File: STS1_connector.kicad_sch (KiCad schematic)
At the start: 2 parts

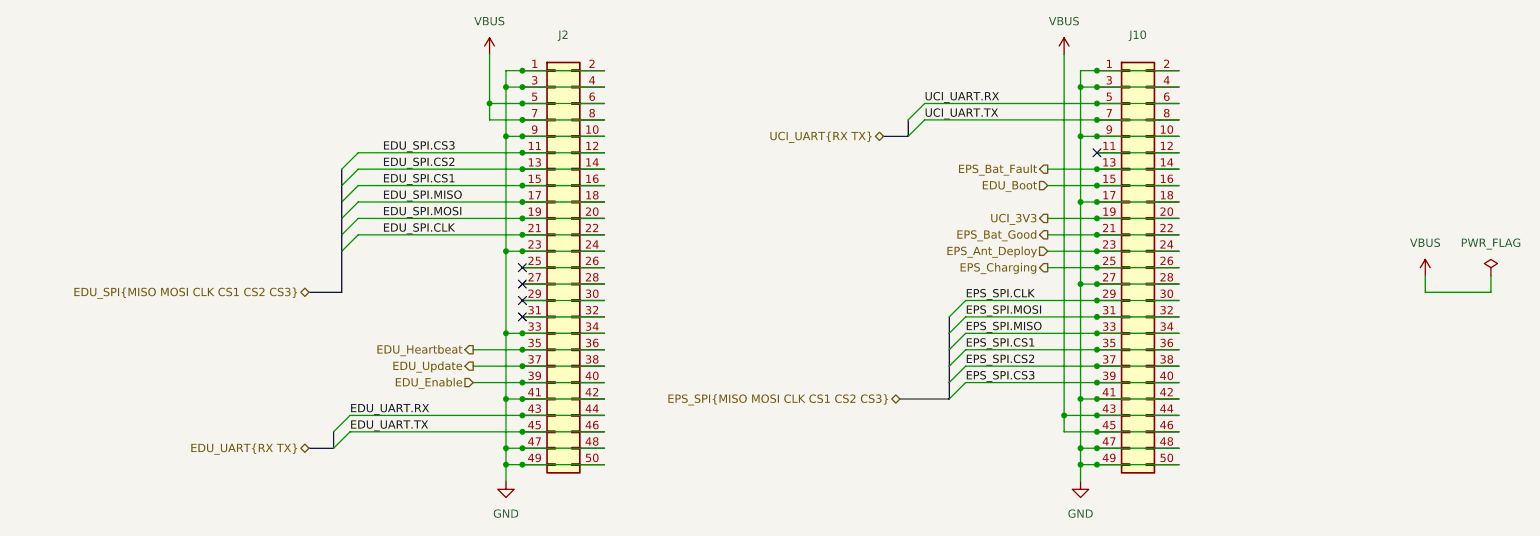
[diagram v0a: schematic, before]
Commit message: Reorganize and clean-up the components around the STM. Pinout changes: 1) Flash_CS moved from PB9 to PA4 2) Dosi_En added on PB10 3) EDU_Boot_Pin added on PB2 4) WDT_Clear moved from PA9 to PB9
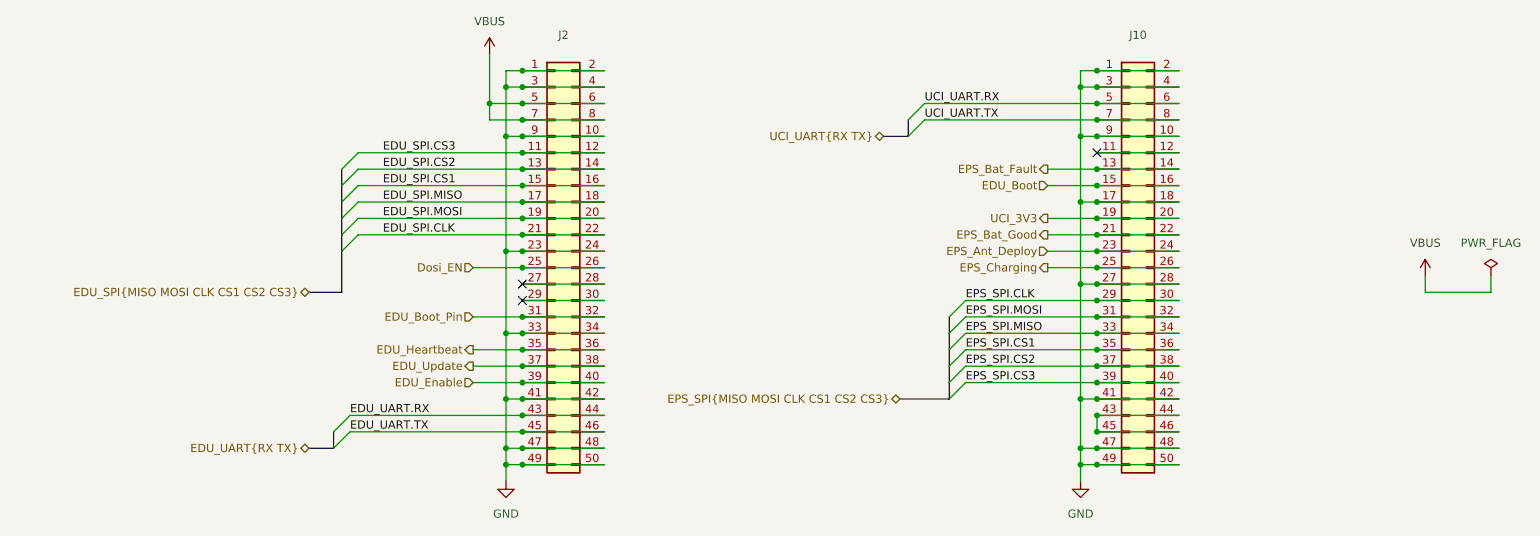
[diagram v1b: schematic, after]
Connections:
- net VBUS: no longer J10.43 (Pin_43), J10.44 (Pin_44), J10.45 (Pin_45), J10.46 (Pin_46)
- net Dosi_EN: now reaches J2.25 (Pin_25), J2.26 (Pin_26)
- net EDU_Boot_Pin: now reaches J2.31 (Pin_31), J2.32 (Pin_32)
- new net: J10.43 (Pin_43), J10.44 (Pin_44), J10.45 (Pin_45), J10.46 (Pin_46)
- no-connect marks 5 -> 3

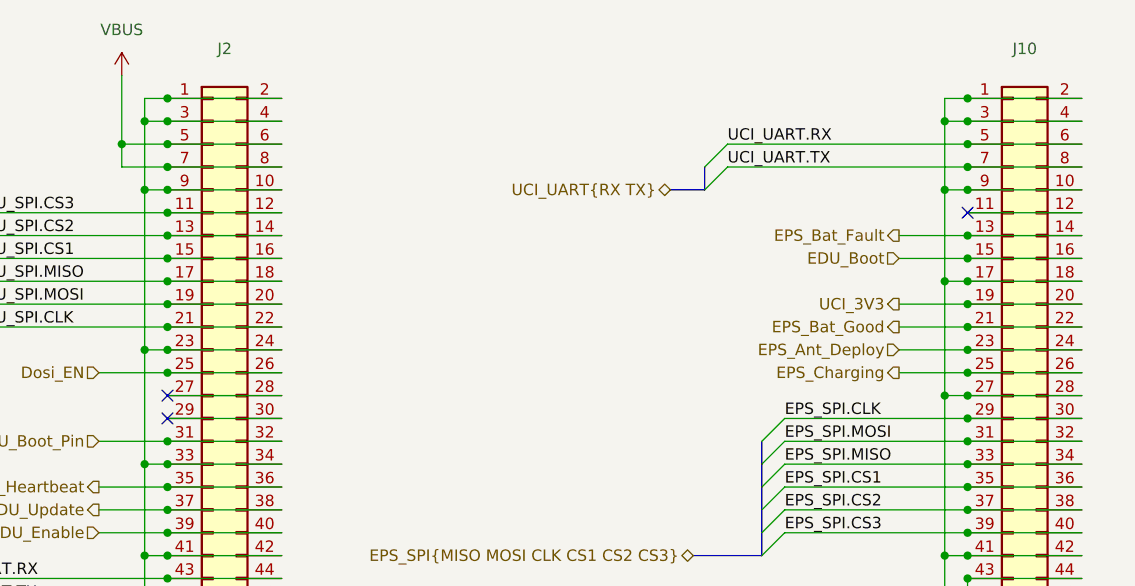
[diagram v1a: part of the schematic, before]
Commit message: Add latchup protection circuits
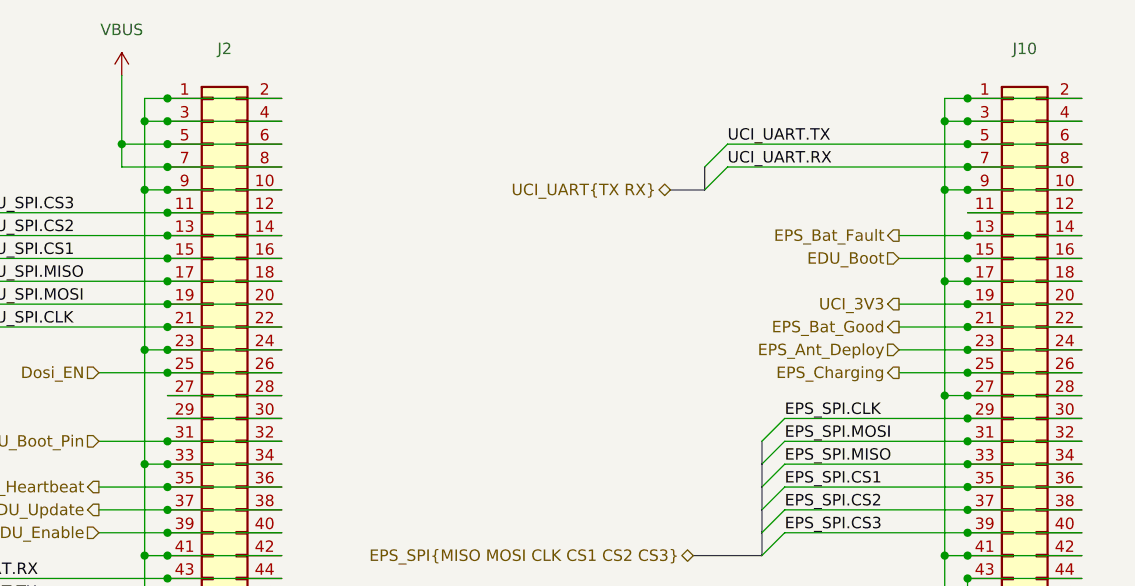
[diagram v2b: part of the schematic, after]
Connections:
- net UCI_UART.RX: now also J10.7 (Pin_7), J10.8 (Pin_8); no longer J10.5 (Pin_5), J10.6 (Pin_6)
- net UCI_UART.TX: now also J10.5 (Pin_5), J10.6 (Pin_6); no longer J10.7 (Pin_7), J10.8 (Pin_8)
- no-connect marks 3 -> 0
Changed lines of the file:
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@@
   (junction (at 173.99 96.52) (diameter 0) (color 0 0 0 0)
   )
-  (no_connect (at 85.09 81.28))
-  (no_connect (at 85.09 78.74))
-  (no_connect (at 173.99 58.42))
   (bus_entry (at 151.13 93.98) (size 2.54 -2.54)
     (stroke (width 0) (type default) (color 0 0 0 0))
@@
     (effects (font (size 1.27 1.27)) (justify left bottom))
   )
-  (label "UCI_UART.TX" (at 147.32 53.34 0)
+  (label "UCI_UART.RX" (at 147.32 53.34 0)
     (effects (font (size 1.27 1.27)) (justify left bottom))
   )
@@
     (effects (font (size 1.27 1.27)) (justify left bottom))
   )
-  (label "UCI_UART.RX" (at 147.32 50.8 0)
+  (label "UCI_UART.TX" (at 147.32 50.8 0)
     (effects (font (size 1.27 1.27)) (justify left bottom))
   )
@@
     (effects (font (size 1.27 1.27)) (justify right))
   )
-  (hierarchical_label "UCI_UART{RX TX}" (shape bidirectional) (at 140.97 55.88 180)
-    (effects (font (size 1.27 1.27)) (justify right))
-  )
+  (hierarchical_label "UCI_UART{TX RX}" (shape bidirectional) (at 140.97 55.88 180)
+    (effects (font (size 1.27 1.27)) (justify right))
+  )

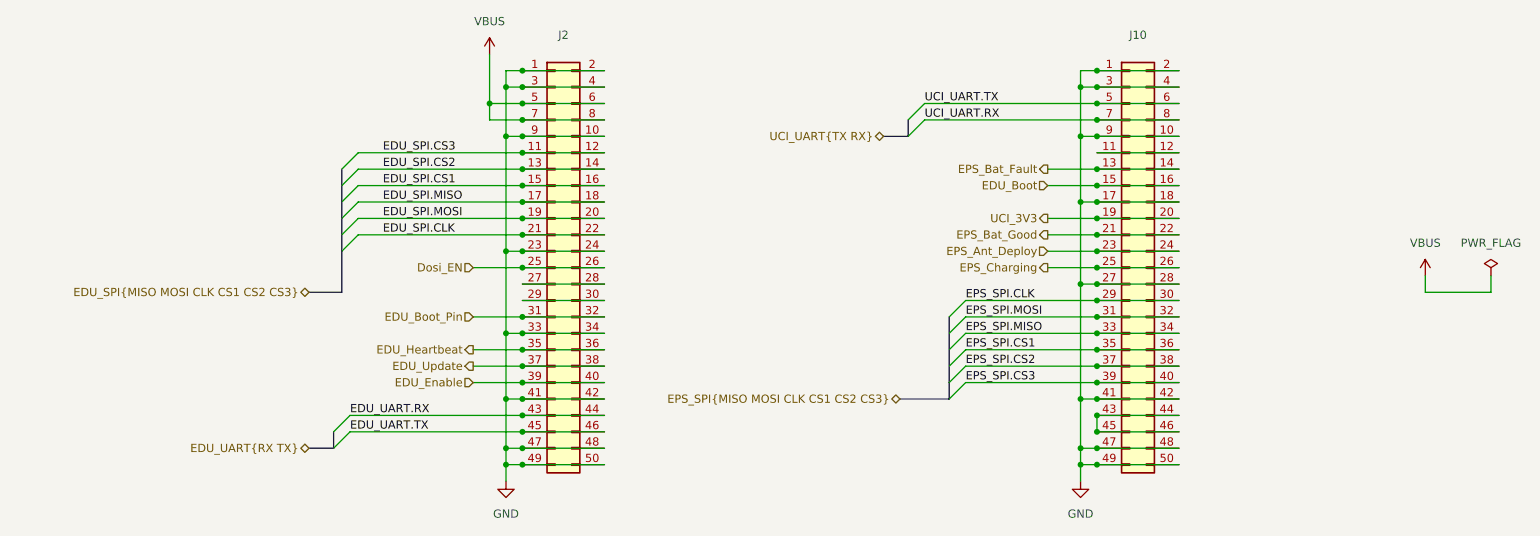
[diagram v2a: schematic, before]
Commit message: Add for new lines to the UCI bus; plus minor fixes: introduce resistor in EDU_BOOT_Pin line, remove zener before DC-DC ~EN input
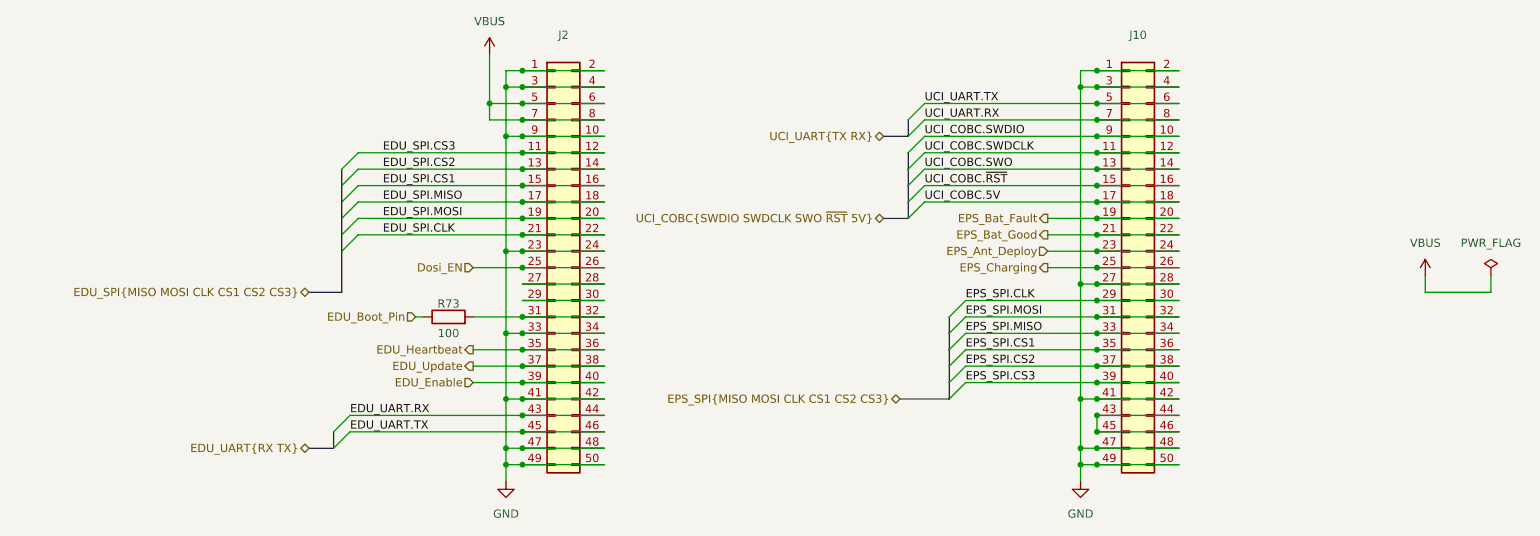
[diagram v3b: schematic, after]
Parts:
- added R73: 100, Resistor_SMD:R_0603_1608Metric, symbol Device:R
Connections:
- net UCI_3V3 is gone; now on net EPS_Bat_Fault: J10.19 (Pin_19), J10.20 (Pin_20)
- net EDU_Boot_Pin: now also R73.1; no longer J2.31 (Pin_31), J2.32 (Pin_32)
- net EPS_Bat_Fault: no longer J10.13 (Pin_13), J10.14 (Pin_14)
- net GND: no longer J10.10 (Pin_10), J10.17 (Pin_17), J10.18 (Pin_18), J10.9 (Pin_9)
- net UCI_COBC.SWDCLK: now reaches J10.11 (Pin_11), J10.12 (Pin_12)
- net EDU_Boot renamed UCI_COBC.~{RST}
- new net: J2.31 (Pin_31), J2.32 (Pin_32), R73.2
- new net UCI_COBC.5V: J10.17 (Pin_17), J10.18 (Pin_18)
- new net UCI_COBC.SWDIO: J10.10 (Pin_10), J10.9 (Pin_9)
- new net UCI_COBC.SWO: J10.13 (Pin_13), J10.14 (Pin_14)

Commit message: Add manufacture number and JLCPCB part number to components
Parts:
- R73: JLCPCB Part # (none) -> C2074896; Manufacturer_Part_Number (none) -> CRS0603AFX-1000ELF
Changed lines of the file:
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@@
+      (effects (font (size 1.27 1.27)) hide)
+    )
+    (property "JLCPCB Part #" "C2074896" (id 4) (at 73.66 83.82 0)
+      (effects (font (size 1.27 1.27)) hide)
+    )
+    (property "Manufacturer_Part_Number" "CRS0603AFX-1000ELF" (id 5) (at 73.66 83.82 0)
       (effects (font (size 1.27 1.27)) hide)
     )

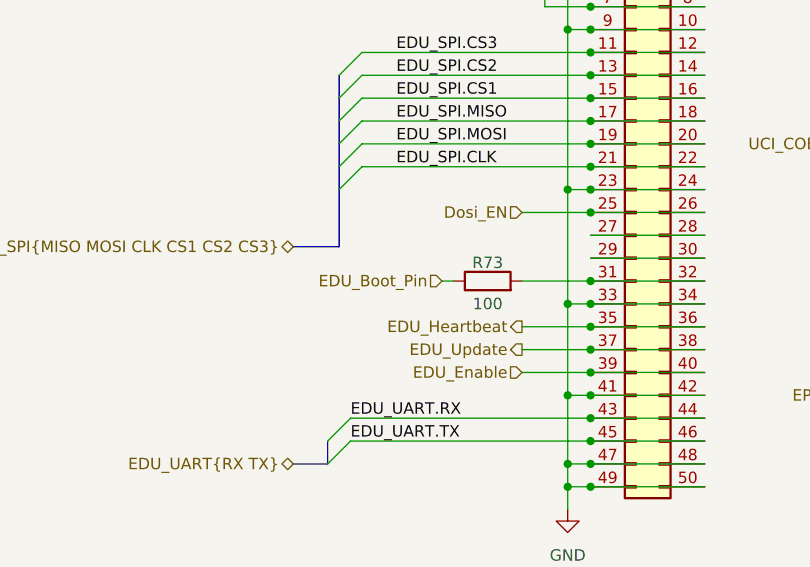
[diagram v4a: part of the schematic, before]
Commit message: Add series resistors to the outputs of STM
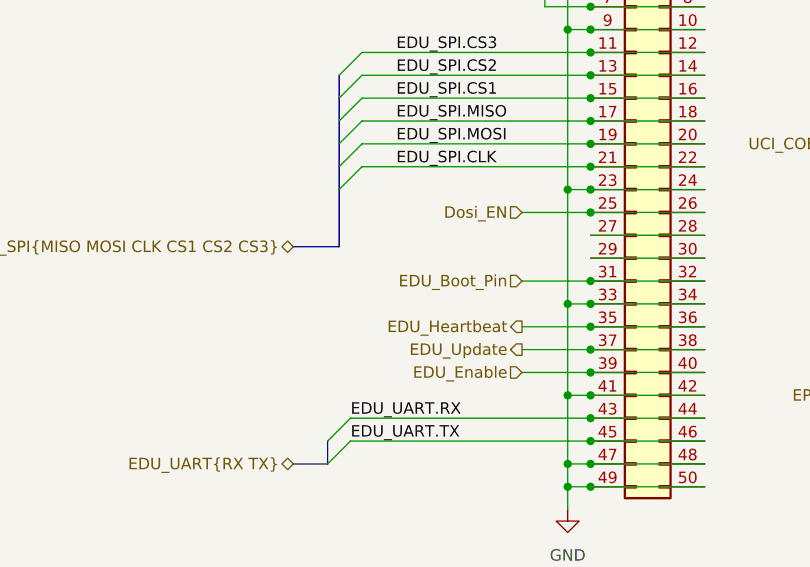
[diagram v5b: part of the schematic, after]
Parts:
- removed R73: 100, Resistor_SMD:R_0603_1608Metric, symbol Device:R
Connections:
- net EDU_Boot_Pin: now also J2.31 (Pin_31), J2.32 (Pin_32)
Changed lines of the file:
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@@
-    (stroke (width 0) (type default) (color 0 0 0 0))
-  )
-  (wire (pts (xy 68.58 83.82) (xy 69.85 83.82))
     (stroke (width 0) (type default) (color 0 0 0 0))
   )
@@
     (effects (font (size 1.27 1.27)) (justify right))
   )
-  (hierarchical_label "EDU_Boot_Pin" (shape input) (at 68.58 83.82 180)
+  (hierarchical_label "EDU_Boot_Pin" (shape input) (at 77.47 83.82 180)
     (effects (font (size 1.27 1.27)) (justify right))
   )
@@
     (pin "1")
   )
-  (symbol (lib_id "Device:R") (at 73.66 83.82 90) (unit 1)
-    (in_bom yes) (on_board yes)
-    (property "Reference" "R73" (id 0) (at 73.66 81.788 90))
-    (property "Value" "100" (id 1) (at 73.66 86.36 90))
-    (property "Footprint" "Resistor_SMD:R_0603_1608Metric" (id 2) (at 73.66 85.598 90)
-      (effects (font (size 1.27 1.27)) hide)
-    )
-    (property "Datasheet" "~" (id 3) (at 73.66 83.82 0)
-      (effects (font (size 1.27 1.27)) hide)
-    )
-    (property "JLCPCB Part #" "C2074896" (id 4) (at 73.66 83.82 0)
-      (effects (font (size 1.27 1.27)) hide)
-    )
-    (property "Manufacturer_Part_Number" "CRS0603AFX-1000ELF" (id 5) (at 73.66 83.82 0)
-      (effects (font (size 1.27 1.27)) hide)
-    )
-    (pin "1")
-    (pin "2")
-  )
   (symbol (lib_id "power:GND") (at 171.45 109.22 0) (unit 1)

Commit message: Exclude R11 (DNP) from position file
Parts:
- J10, J2: now left out of the parts list
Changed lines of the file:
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@@
   )
   (symbol (lib_id "Connector_Generic:Conn_02x25_Odd_Even") (at 90.17 76.2 0) (unit 1)
-    (in_bom yes) (on_board yes)
+    (in_bom no) (on_board yes)
     (property "Reference" "J2" (id 0) (at 91.44 40.2082 0))
     (property "Value" "~" (id 1) (at 91.44 42.5196 0))
@@
   )
   (symbol (lib_id "Connector_Generic:Conn_02x25_Odd_Even") (at 179.07 76.2 0) (unit 1)
-    (in_bom yes) (on_board yes)
+    (in_bom no) (on_board yes)
     (property "Reference" "J10" (id 0) (at 180.34 40.2082 0))
     (property "Value" "~" (id 1) (at 180.34 42.5196 0))

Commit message: Update kicad files to v10.0 from v9.0
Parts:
- J10, J2: value ~ -> (none)
